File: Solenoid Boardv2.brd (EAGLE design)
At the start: 76.2 x 31.8 mm, 52 parts, among them Y2 ECS-80-S-4X

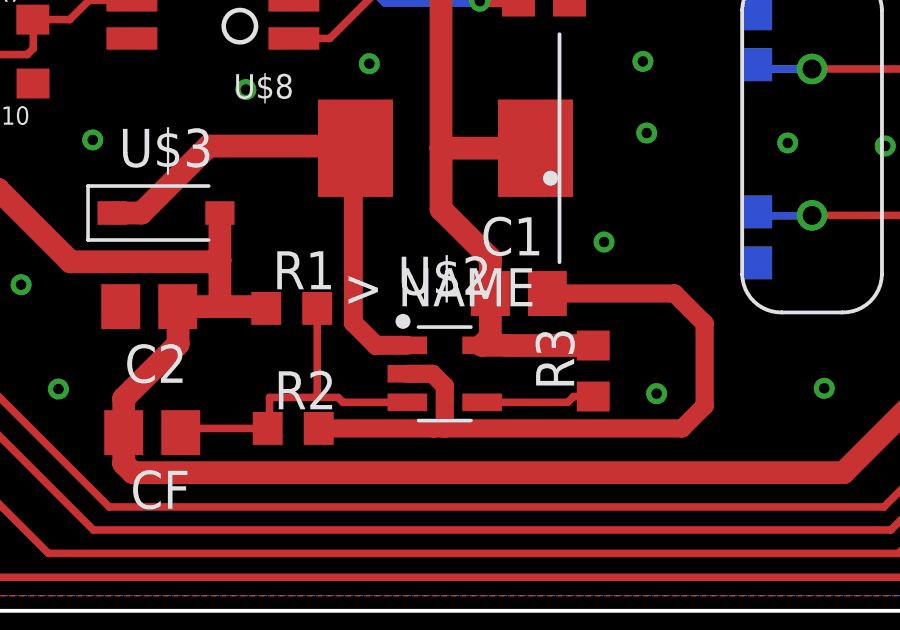
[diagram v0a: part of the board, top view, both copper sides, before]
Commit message: revised boost converter resistors and added data sheet for boost converter
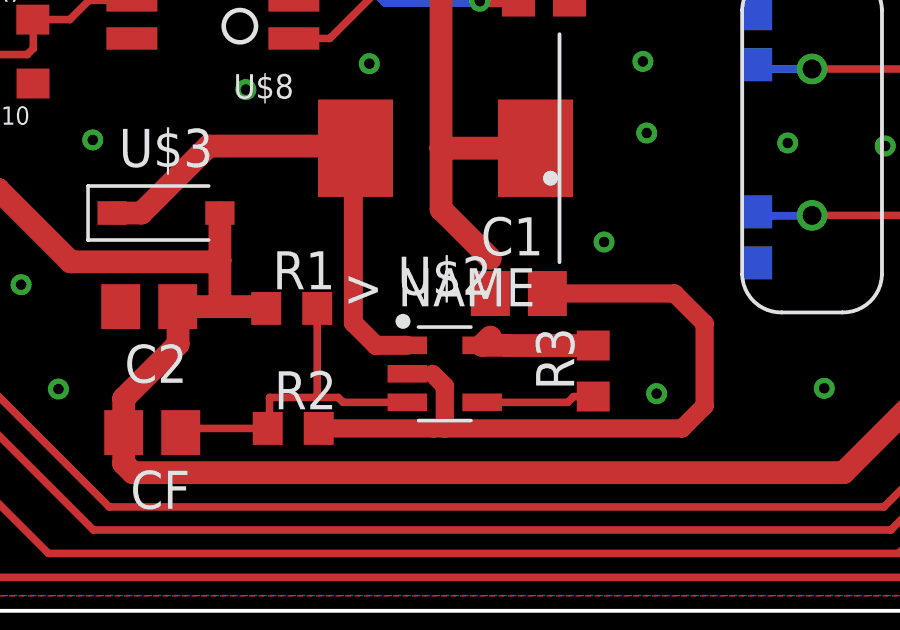
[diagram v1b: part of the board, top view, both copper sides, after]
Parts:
- R1: value 13.3k -> 220k
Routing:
- net +12V: track 107.0 -> 104.4 mm
- net GND: track 37.8 -> 37.0 mm
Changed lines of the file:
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@@
 <attribute name="VALUE" x="69.95" y="-1.143" size="1.27" layer="27"/>
 </element>
-<element name="R1" library="rcl" library_urn="urn:adsk.eagle:library:334" package="R0603" package3d_urn="urn:adsk.eagle:package:23555/2" value="13.3k" x="24.87" y="10.08">
+<element name="R1" library="rcl" library_urn="urn:adsk.eagle:library:334" package="R0603" package3d_urn="urn:adsk.eagle:package:23555/2" value="220k" x="24.87" y="10.08">
 <attribute name="NAME" x="24.235" y="10.715" size="1.27" layer="25"/>
 <attribute name="SPICEPREFIX" value="R" x="74.4" y="-45.8" size="1.778" layer="27" display="off"/>
@@
 <signal name="GND">
 <contactref element="C1" pad="2"/>
-<contactref element="U$2" pad="2"/>
 <contactref element="R2" pad="2"/>
 <contactref element="U$1" pad="GND"/>
 <contactref element="C3" pad="2"/>
 <contactref element="U$5" pad="1"/>
-<contactref element="C2" pad="2"/>
 <contactref element="C13" pad="2"/>
 <contactref element="C15" pad="2"/>
@@
 <wire x1="53.4924" y1="20.4216" x2="54.8132" y2="20.4216" width="0.381" layer="1"/>
 <wire x1="53.05" y1="19.9792" x2="53.4924" y2="20.4216" width="0.381" layer="1"/>
-<wire x1="28.7237" y1="7.9" x2="29.565" y2="7.9" width="0.6096" layer="1"/>
 <wire x1="29.565" y1="7.9" x2="29.972" y2="7.493" width="0.6096" layer="1"/>
 <wire x1="29.6004" y1="6.08" x2="25.77" y2="6.08" width="0.6096" layer="1"/>
@@
 <wire x1="37.6324" y1="10.5768" x2="38.6334" y2="9.5758" width="0.6096" layer="1"/>
 <wire x1="29.972" y1="7.493" x2="29.972" y2="6.08" width="0.6096" layer="1"/>
+<contactref element="U$2" pad="2"/>
+<contactref element="C2" pad="2"/>
+<wire x1="29.565" y1="7.9" x2="28.7237" y2="7.9" width="0" layer="19" extent="1-1"/>
 </signal>
 <signal name="+12V">
@@
 <contactref element="R3" pad="2"/>
 <contactref element="I1" pad="1"/>
-<contactref element="C1" pad="1"/>
 <contactref element="JP9" pad="1"/>
 <contactref element="C4" pad="1"/>
@@
 <wire x1="29.8486" y1="15.42" x2="29.8486" y2="13.3886" width="0.762" layer="1"/>
 <wire x1="29.8486" y1="13.3886" x2="31.492" y2="11.7452" width="0.762" layer="1"/>
-<wire x1="31.492" y1="10.5768" x2="31.492" y2="9.1257" width="0.762" layer="1"/>
 <wire x1="31.492" y1="9.1257" x2="31.2163" y2="8.85" width="0.762" layer="1"/>
-<wire x1="31.492" y1="11.7452" x2="31.492" y2="10.5768" width="0.762" layer="1"/>
 <wire x1="22.8716" y1="27.85" x2="21.3868" y2="26.3652" width="0.762" layer="1"/>
 <wire x1="21.3868" y1="26.3652" x2="21.3868" y2="24.0284" width="0.762" layer="1"/>
+<contactref element="C1" pad="1"/>
+<wire x1="31.492" y1="11.7452" x2="31.492" y2="10.5768" width="0" layer="19" extent="1-1"/>
+<wire x1="31.492" y1="9.1257" x2="31.492" y2="10.5768" width="0" layer="19" extent="1-1"/>
 </signal>
 <signal name="+24V">
